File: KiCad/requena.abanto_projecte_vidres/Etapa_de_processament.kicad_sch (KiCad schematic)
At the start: 15 parts, among them U1 PIC18F23K20_ISS, Y2 Crystal

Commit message: arreglos
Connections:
- net Vcc: now also U1.13 (VDD); no longer U1.11 (SOSCI/RP4/CN1/PMBE/RB4)
- net INB: now reaches U1.12 (SOSCO/T1CK/CN0/PMA1/RA4)
- net PIN_DIGITAL1: now reaches U1.14 (PGED3/ASDA1/RP5/CN27/PMD7/RB5)
- net PIN_DIGITAL2: now reaches U1.15 (PGEC3/ASCL1/RP6/CN24/PMD6/RB6)
- net IRQ: now reaches U1.16 (INT0/RP7/CN23/PMD5/RB7)
- net MOSI: now reaches U1.17 (TCK/SCL1/RP8/CN22/PMD4/RB8)
- net SCK: now reaches U1.18 (TDO/SDA1/RP9/CN21/PMD3/RB9)
- net AN0: now reaches U1.2 (RA0/AN0/CN2/Vref+)
- net PWM: now reaches U1.25 (AN10/RTCC/RP14/CN12/PMWR/RB14)
- net MISO: now reaches U1.4 (PGED1/AN2/C2IN-/RP0/CN4/RB0)
- net NRSTPD: now reaches U1.5 (PGEC1/_AN3/C2IN+/RP1/CN5/RB1)
- net OPEN_FC: now reaches U1.6 (AN4/C1IN-/RP2/CN6/RB2)
- net CLOSED_FC: now reaches U1.7 (AN5/C1IN+/RP3/CN7/RB3)
- new net INA: U1.11 (SOSCI/RP4/CN1/PMBE/RB4)
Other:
- moved on the sheet: C1, C2, C3, C5, C6, C7, D1, D2, R1, R2, R3, R4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

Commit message: clase
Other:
- note added: "MUX o PIC 44 pins"
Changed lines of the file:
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@@
 	(generator_version "9.0")
 	(paper "A4")
+	(text "MUX o PIC 44 pins\n"
+		(exclude_from_sim no)
+		(at 95.758 133.35 0)
+		(effects
+			(font
+				(size 1.27 1.27)
+			)
+		)
+	)
 	(junction
 		(at 212.09 76.2)

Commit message: cambios de clase
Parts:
- added U2: NMUX1308PW, Package_SO:TSSOP-16_4.4x5mm_P0.65mm, symbol Analog_Switch:NMUX1308PW
- U1: value PIC18F23K20_ISS -> PIC24HJ128GP502
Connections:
- net CLOSED_FC: now also U2.1 (Y4), U2.2 (Y6); no longer U1.7 (AN5/C1IN+/RP3/CN7/RB3)
- net CLOSE_D: now also U2.13 (Y0)
- net DOWN_W: now also U2.15 (Y2)
- net GND: now also U2.6 (~{E}), U2.8 (GND)
- net OPEN_D: now also U2.14 (Y1)
- net OPEN_FC: now also U2.4 (Y7), U2.5 (Y5); no longer U1.6 (AN4/C1IN-/RP2/CN6/RB2)
- net UP_W: now also U2.12 (Y3)
- net Vcc: now also U2.16 (V_{CC})
- new net MUX: U1.7 (AN5/C1IN+/RP3/CN7/RB3), U2.3 (Z)
- new net S0: U2.11 (S0)
- new net S1: U2.10 (S1)
- new net S2: U2.9 (S2)
- no-connect marks 0 -> 2
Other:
- note removed: "MUX o PIC 44 pins"

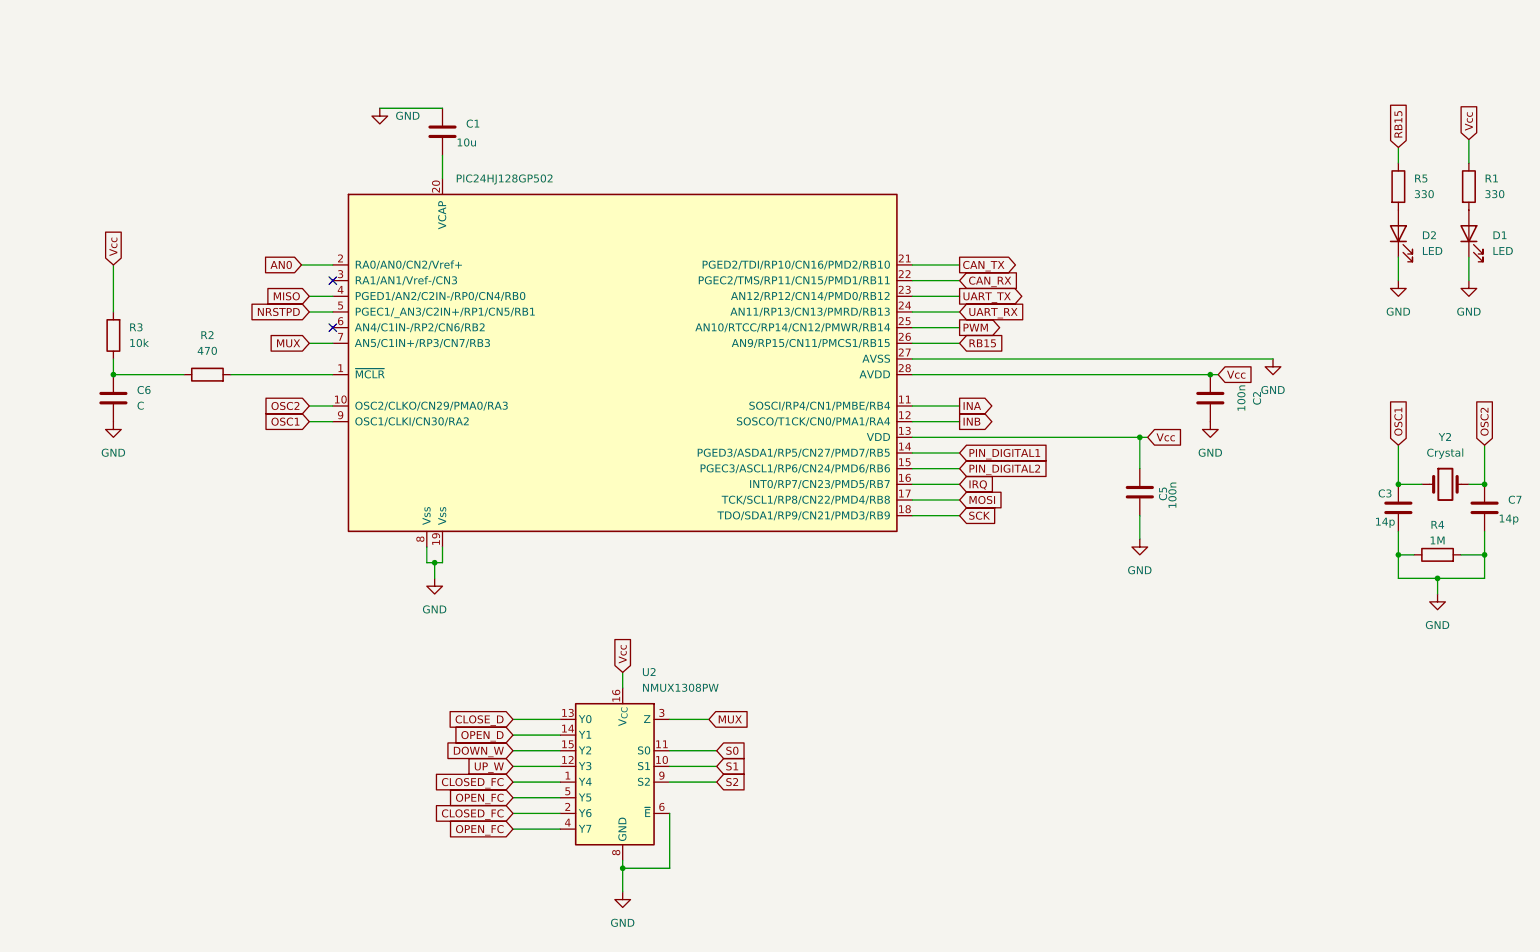
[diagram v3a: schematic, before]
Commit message: millora el esquematic
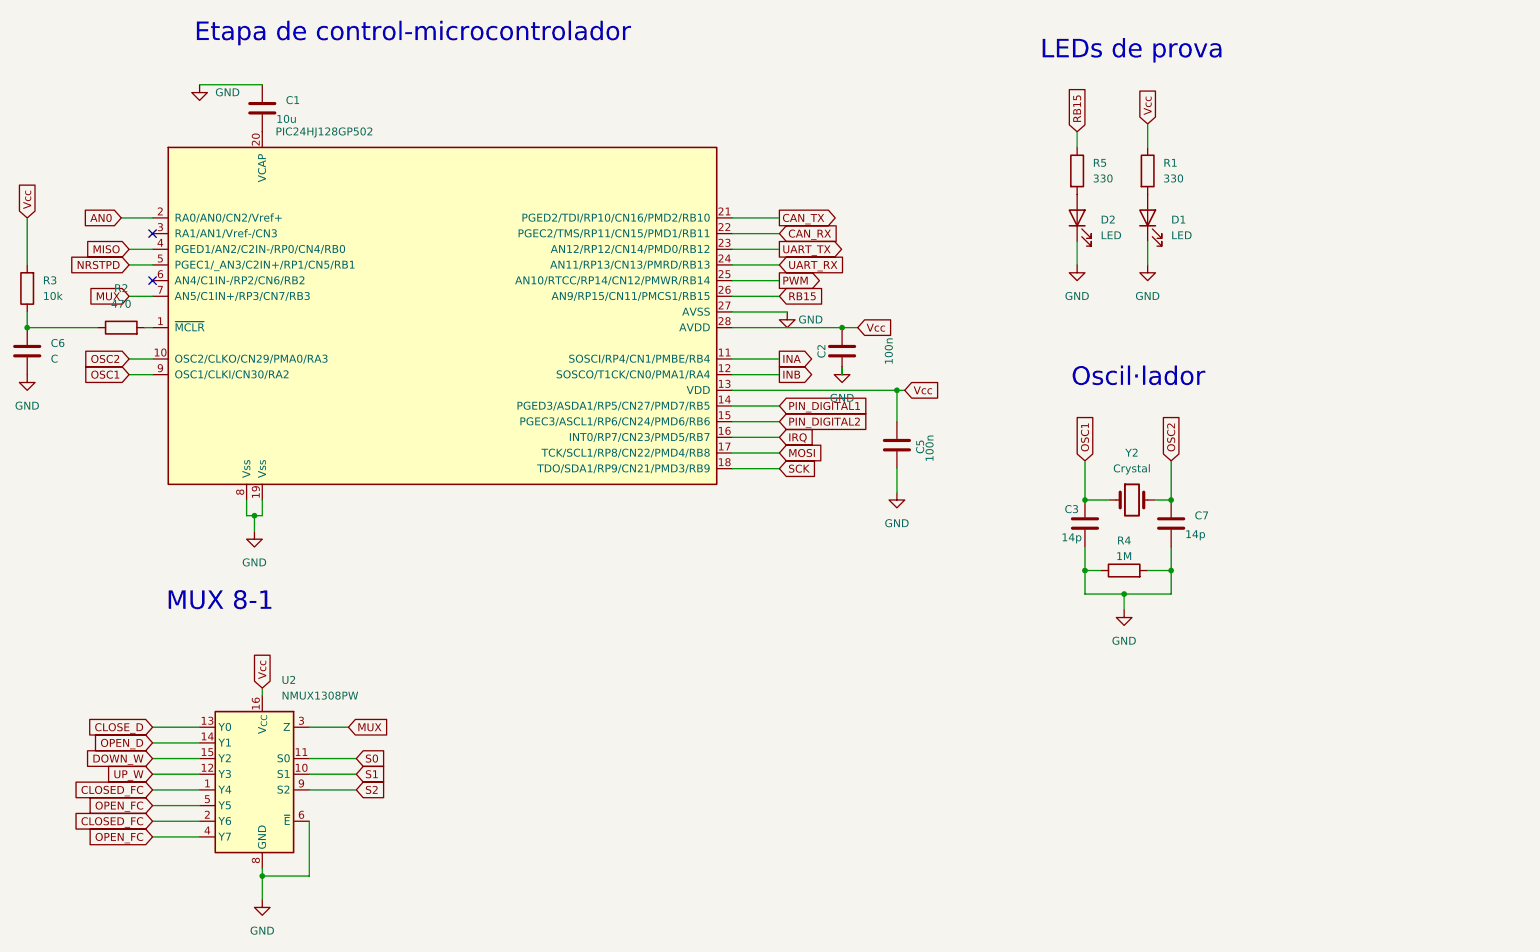
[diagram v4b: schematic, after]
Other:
- note added: "Etapa de control-microcontrolador"
- note added: "LEDs de prova"
- note added: "MUX 8-1"
- note added: "Oscil·lador"
- moved on the sheet: C1, C2, C3, C5, C6, C7, D1, D2, R1, R2, R3, R4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

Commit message: Millora projecte 1
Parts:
- removed C6: C, symbol Device:C
- removed R4: 1M, symbol Device:R
- added C4: 100n, symbol Device:C
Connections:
- net GND: now also C1.2, C4.2; no longer C1.1
- net at R2.1, R3.1: now also C4.1
- net at U1.20 (VCAP): now also C1.1; no longer C1.2
- net PIN_DIGITAL1: no longer names the net of U1.14 (RP5/RB5)
- net PIN_DIGITAL2: no longer names the net of U1.15 (RP6/RB6)
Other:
- moved on the sheet: C1, C2, C3, C5, C7, D1, D2, R1, R2, R3, R5, U2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

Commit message: millora
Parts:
- removed C4: 100n, symbol Device:C
- removed R3: 10k, symbol Device:R
- added C10: 100nF, symbol Device:C
- added C11, C12: C, symbol Device:C
- added C6 (x2), C8 (x2), C9: 100nF, symbol Device:C_Small
- added J1, J2: DE9_Pins, symbol Connector:DE9_Pins
- added J3: Conn_01x05, symbol Connector_Generic:Conn_01x05
- added JP1: Jumper_3_Open, symbol Jumper:Jumper_3_Open
- added R4: 120, symbol Device:R
- added SW1, SW3, SW4, SW5: SW_Omron_B3FS, symbol Switch:SW_Omron_B3FS
- added SW2: SW_Push_SPDT, symbol Switch:SW_Push_SPDT
- added SW6: SW_Push, symbol Switch:SW_Push
- added U3: TJA1051TK-3, Package_SON:HVSON-8-1EP_3x3mm_P0.65mm_EP1.6x2.4mm, symbol Interface_CAN_LIN:TJA1051TK-3
- added U4: PN5120A0HN1, Package_DFN_QFN:HVQFN-32-1EP_5x5mm_P0.5mm_EP3.1x3.1mm, symbol RF_RFID:PN5120A0HN1
- added Y1: Crystal, symbol Device:Crystal
- R2: value 470 -> R
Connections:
- net CAN_RX: now also U3.4 (RXD)
- net CAN_TX: now also U3.1 (TXD)
- net CLOSED_FC: now also SW2.3 (C)
- net CLOSE_D: now also SW5.2
- net DOWN_W: now also SW3.2
- net GND: now also C10.2, C11.2, C12.2, C6.1, C6.1, C8.1, C8.1, C9.1, J1.5, J2.3, J2.6, J3.3 (Pin_3), SW1.1, SW3.1, SW4.1, SW5.1, SW6.2, U3.2 (GND), U3.8 (S), U3.9 (GND), U4.1 (A1), U4.10 (TVSS), U4.14 (TVSS), U4.18 (AVSS), U4.24 (ALE), U4.32 (A0), U4.33 (EP), U4.4 (DVSS), U4.5 (PVSS)
- net IRQ: now also U4.23 (IRQ)
- net MISO: now also U1.15 (RP6/RB6), U4.17 (RX); no longer U1.4 (RP0/RB0)
- net MOSI: now also U4.11 (TX1)
- net NRSTPD: now also U1.14 (RP5/RB5), U4.6 (~{NRSTPD}); no longer U1.5 (RP1/RB1)
- net OPEN_D: now also SW4.2
- net OPEN_FC: now also SW2.1 (A)
- net SCK: now also U4.13 (TX2)
- net UART_RX: now also J1.2
- net UART_TX: now also J1.3
- net UP_W: now also SW1.2
- net Vcc: no longer C2.1, C5.1, U1.13 (VDD), U1.28 (AVDD), U2.16 (V_{CC})
- net at R2.1: now also JP1.3 (B), SW6.1
- net at U1.1 (~{MCLR}): now also JP1.2 (C); no longer R2.2
- new net: J2.2, R4.2, U3.6 (CANL)
- new net: J2.7, R4.1, U3.7 (CANH)
- new net: C11.1, U4.21 (OSCIN), Y1.1
- new net: C12.1, U4.22 (OSCOUT), Y1.2
- new net: C10.1, U4.16 (VMID)
- new net: J3.1 (Pin_1), JP1.1 (A)
- new net PGEC1: J3.5 (Pin_5), U1.5 (RP1/RB1)
- new net PGED1: J3.4 (Pin_4), U1.4 (RP0/RB0)
- new net VCC: C2.1, C5.1, C6.2, C6.2, C8.2, C8.2, C9.2, J3.2 (Pin_2), R2.2, SW2.2 (B), U1.13 (VDD), U1.28 (AVDD), U2.16 (V_{CC}), U3.5 (VIO), U4.12 (TVDD), U4.15 (AVDD), U4.2 (PVDD), U4.3 (DVDD), U4.9 (SVDD)
- new net V_OUT_DCDC: U3.3 (VCC)
- no-connect marks 2 -> 20
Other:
- note added: "A L'ANTENA =>>>Chip antena"
- note added: "CAN"
- note added: "Final de carrera-botonera"
- note added: "LECTOR RFID"
- note added: "USART"
- moved on the sheet: C1, C2, C5

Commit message: guardado
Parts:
- renumbered C7 to C?, C5 to C?, C6 to C?, C1 to C?, C8 to C?, C10 to C?, C3 to C?, C12 to C?, C2 to C?, C9 to C?, C11 to C?, D2 to D?, D1 to D?, J1 to J?, J2 to J?, J3 to J?, JP1 to JP?, R5 to R?, R1 to R?, R4 to R?, R2 to R?, SW5 to SW?, SW6 to SW?, SW2 to SW?, SW4 to SW?, SW1 to SW?, SW3 to SW?, U3 to U?, U2 to U?, U1 to U?, U4 to U?, Y1 to Y?, Y2 to Y?

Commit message: cambios
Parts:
- removed C?: 100nF, symbol Device:C
- added C? (x3): 100n, symbol Device:C
- added C?: 100nF, symbol Device:C_Small
- added J?: Conn_01x04_Socket, symbol Connector:Conn_01x04_Socket
- added R? (x6): 10k, symbol Device:R
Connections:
- net Vcc is gone; now on net VCC: R?.1
- net CLOSED_FC: now also R?.1
- net CLOSE_D: now also R?.1
- net DOWN_W: now also R?.1
- net GND: now also JP?.2 (C), SW?.2 (B), U?.1 (~{MCLR}), C?.1, C?.2, C?.2, C?.2
- net OPEN_D: now also R?.1
- net OPEN_FC: now also R?.1
- net UP_W: now also R?.1
- net VCC: now also C?.1, C?.1, R?.2, R?.2, R?.2, R?.2, R?.2, R?.2; no longer SW?.2 (B)
- net at U?.16 (VMID): now also C?.2
- net at U?.19 (AUX1): now also J?.3 (Pin_3)
- net at U?.20 (AUX2): now also J?.4 (Pin_4)
- net at U?.7 (SIGIN): now also J?.1 (Pin_1)
- net at U?.8 (SIGOUT): now also J?.2 (Pin_2)
- net V_OUT_DCDC renamed +5V
- net +5V: now also C?.1
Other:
- note added: "microcontrolador"
- note removed: "A L'ANTENA =>>>Chip antena"
- note removed: "Etapa de control-microcontrolador"
- note removed: "Oscil·lador"
- moved on the sheet: C?, D?, J?, JP?, R?, SW?, U?, Y?
